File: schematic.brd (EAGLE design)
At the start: 100 x 70 mm, 44 parts, among them U1 ADP3338AKCZ-3.3RL7

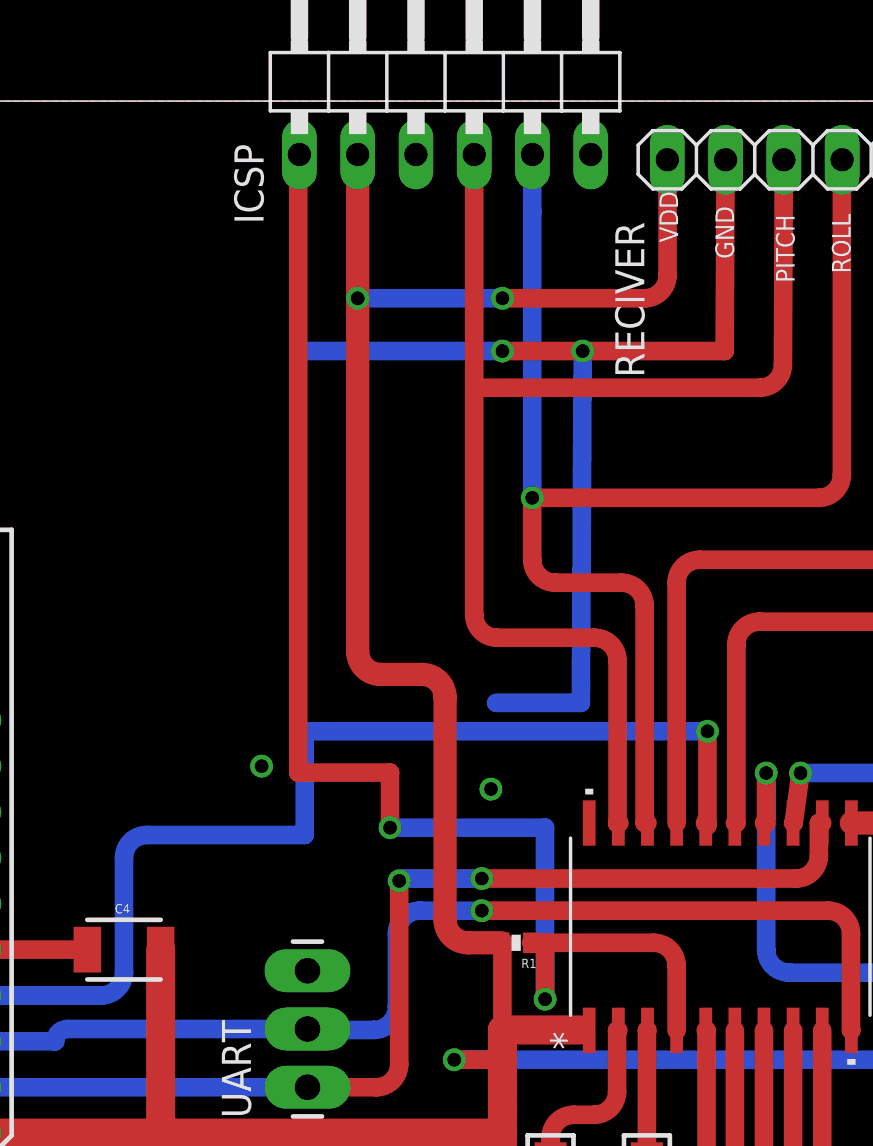
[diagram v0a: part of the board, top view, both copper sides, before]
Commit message: Reversed ICSP pins so programmer will be right way up
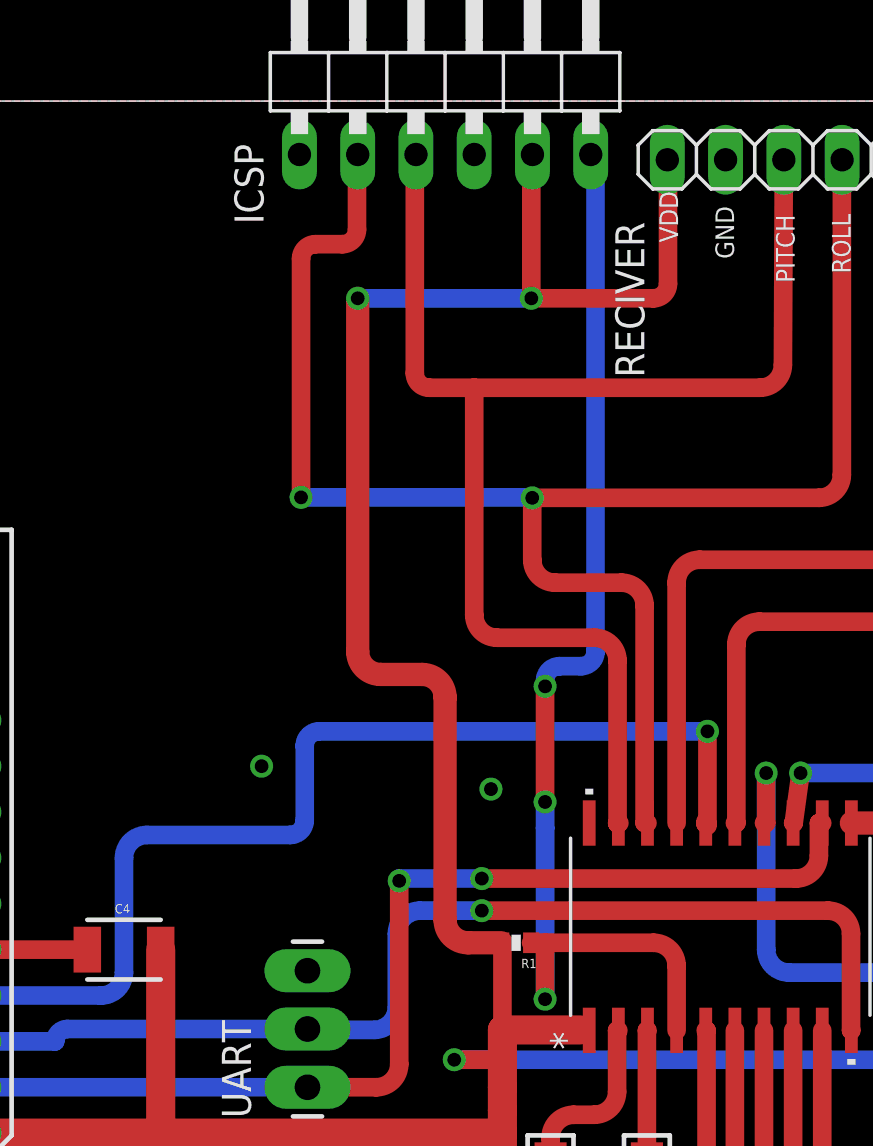
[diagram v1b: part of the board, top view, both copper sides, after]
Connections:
- net GND: now also ICSP.4; no longer ICSP.3
- net LVP: now also ICSP.1; no longer ICSP.6
- net PGC/ROLL: now also ICSP.2; no longer ICSP.5
- net PGD/PITCH: now also ICSP.3; no longer ICSP.4
- net VDD: now also ICSP.5; no longer ICSP.2
- net VPP: now also ICSP.6; no longer ICSP.1
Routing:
- net GND: track 60.0 -> 14.1 mm, vias 6 -> 4
- net PGC/ROLL: track 61.8 -> 73.6 mm, vias 1 -> 2
- net VPP: track 59.7 -> 50.5 mm, vias 2 -> 3
- net PGD/PITCH: track 57.2 -> 59.5 mm
- net XBEE_INT: track 46.1 -> 45.4 mm
- net VDD: track 250.9 -> 250.2 mm
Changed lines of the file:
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@@
 <wire x1="46.4" y1="16.2" x2="46.4" y2="16" width="0.4064" layer="1"/>
 <wire x1="46.5" y1="26.6" x2="46.5" y2="27" width="1.016" layer="1"/>
-<contactref element="ICSP" pad="2"/>
 <wire x1="44" y1="44" x2="43" y2="45" width="1.016" layer="1" curve="90"/>
 <wire x1="43" y1="45" x2="41.19" y2="45" width="1.016" layer="1"/>
@@
 <wire x1="31.6" y1="33" x2="31.6" y2="25.2" width="1.27" layer="1"/>
 <wire x1="31.6" y1="25" x2="31.6" y2="25.2" width="0.6096" layer="1"/>
-<wire x1="40.19" y1="61.4" x2="40.19" y2="67.67" width="1.016" layer="1"/>
 <wire x1="48" y1="16" x2="46.4" y2="16" width="1.27" layer="1"/>
 <wire x1="48" y1="16" x2="48" y2="14.6" width="1.27" layer="1"/>
-<wire x1="53.69" y1="67.44" x2="53.7" y2="68" width="0.8128" layer="1"/>
-<wire x1="53.7" y1="68" x2="53.7" y2="62.4" width="0.8128" layer="1"/>
-<wire x1="53.7" y1="62.4" x2="52.7" y2="61.4" width="0.8128" layer="1" curve="-90"/>
-<wire x1="52.7" y1="61.4" x2="46.5" y2="61.4" width="0.8128" layer="1"/>
-<via x="46.5" y="61.4" extent="1-16" drill="0.6"/>
-<wire x1="46.5" y1="61.4" x2="40.19" y2="61.4" width="0.8128" layer="16"/>
 <via x="40.19" y="61.4" extent="1-16" drill="0.6"/>
 <wire x1="65.05" y1="25.5" x2="65.05" y2="28.2" width="0.8128" layer="1"/>
@@
 <wire x1="74.1" y1="2.4" x2="74" y2="2.4" width="0.254" layer="1"/>
 <wire x1="74" y1="2.4" x2="74" y2="2" width="0.254" layer="1"/>
+<contactref element="ICSP" pad="5"/>
+<wire x1="47.81" y1="67.67" x2="47.76" y2="67.67" width="0.8128" layer="1"/>
+<wire x1="47.76" y1="67.67" x2="47.76" y2="61.4" width="0.8128" layer="1"/>
+<via x="47.76" y="61.4" extent="1-16" drill="0.6" shape="square"/>
+<wire x1="47.76" y1="61.4" x2="40.16" y2="61.4" width="0.8128" layer="16"/>
+<wire x1="40.16" y1="61.4" x2="40.16" y2="61.44" width="0.8128" layer="16"/>
+<wire x1="53.69" y1="67.44" x2="53.72" y2="67.44" width="0.8128" layer="1"/>
+<wire x1="53.72" y1="67.44" x2="53.72" y2="62.035" width="0.8128" layer="1"/>
+<wire x1="53.72" y1="62.035" x2="53.085" y2="61.4" width="0.8128" layer="1" curve="-90"/>
+<wire x1="53.085" y1="61.4" x2="47.72" y2="61.4" width="0.8128" layer="1"/>
+<wire x1="47.76" y1="61.4" x2="47.72" y2="61.4" width="0" layer="19" extent="1-1"/>
+<wire x1="40.19" y1="61.4" x2="40.16" y2="61.4" width="0" layer="19" extent="16-16"/>
 </signal>
 <signal name="VPP">
@@
 <wire x1="53.095" y1="33.3" x2="54.095" y2="32.3" width="0.8128" layer="1" curve="-90"/>
 <wire x1="54.095" y1="32.3" x2="54.095" y2="29.4788" width="0.8128" layer="1"/>
-<contactref element="ICSP" pad="1"/>
-<wire x1="37.65" y1="67.67" x2="37.6" y2="67.67" width="0.8128" layer="1"/>
-<wire x1="37.6" y1="67.67" x2="37.6" y2="40.72" width="0.8128" layer="1"/>
-<wire x1="37.6" y1="40.72" x2="41.6" y2="40.72" width="0.8128" layer="1"/>
-<wire x1="41.6" y1="40.72" x2="41.6" y2="38.32" width="0.8128" layer="1"/>
-<via x="41.6" y="38.32" extent="1-16" drill="0.6" shape="square"/>
-<wire x1="41.6" y1="38.32" x2="48.36" y2="38.32" width="0.8128" layer="16"/>
-<wire x1="48.36" y1="38.32" x2="48.36" y2="30.84" width="0.8128" layer="16"/>
+<wire x1="48.36" y1="38.32" x2="48.36" y2="38.28" width="0.8128" layer="16"/>
 <via x="48.36" y="30.84" extent="1-16" drill="0.6" shape="square"/>
+<wire x1="48.36" y1="38.28" x2="48.36" y2="30.84" width="0.8128" layer="16"/>
 <wire x1="48.36" y1="30.84" x2="48.36" y2="33.3" width="0.8128" layer="1"/>
+<contactref element="ICSP" pad="6"/>
+<wire x1="50.35" y1="67.67" x2="50.56" y2="67.67" width="0.8128" layer="16"/>
+<wire x1="50.56" y1="67.67" x2="50.56" y2="45.995" width="0.8128" layer="16"/>
+<wire x1="50.56" y1="45.995" x2="49.925" y2="45.36" width="0.8128" layer="16" curve="-90"/>
+<wire x1="49.925" y1="45.36" x2="48.995" y2="45.36" width="0.8128" layer="16"/>
+<wire x1="48.995" y1="45.36" x2="48.36" y2="44.725" width="0.8128" layer="16" curve="90"/>
+<wire x1="48.36" y1="44.725" x2="48.36" y2="44.48" width="0.8128" layer="16"/>
+<via x="48.36" y="44.48" extent="1-16" drill="0.6" shape="square"/>
+<wire x1="48.36" y1="44.48" x2="48.36" y2="39.44" width="0.8128" layer="1"/>
+<via x="48.36" y="39.44" extent="1-16" drill="0.6" shape="square"/>
+<wire x1="48.36" y1="39.44" x2="48.36" y2="38.32" width="0.8128" layer="16"/>
 </signal>
 <signal name="N$2">
@@
 <contactref element="D12" pad="C"/>
 <contactref element="UART" pad="3"/>
-<wire x1="50" y1="59.1" x2="49.92" y2="43.76" width="0.8128" layer="16"/>
-<wire x1="49.92" y1="43.76" x2="46.22" y2="43.76" width="0.8128" layer="16"/>
 <wire x1="48" y1="11.4" x2="48" y2="9" width="1.016" layer="1"/>
 <wire x1="48" y1="9" x2="50.19" y2="9" width="1.016" layer="1"/>
 <wire x1="50.19" y1="9" x2="50.19" y2="4.27" width="1.016" layer="1"/>
-<via x="50" y="59.1" extent="1-16" drill="0.6"/>
-<wire x1="50" y1="59.1" x2="46.5" y2="59.1" width="0.8128" layer="1"/>
-<via x="46.5" y="59.1" extent="1-16" drill="0.6"/>
-<wire x1="46.5" y1="59.1" x2="37.65" y2="59.1" width="0.8128" layer="16"/>
-<wire x1="50" y1="59.1" x2="56.19" y2="59.1" width="0.8128" layer="1"/>
-<wire x1="56.19" y1="59.1" x2="56.23" y2="67.44" width="0.8128" layer="1"/>
 <polygon width="0.4064" layer="16">
 <vertex x="0" y="70"/>
@@
 <via x="37" y="9.8" extent="1-16" drill="0.6"/>
 <via x="36" y="41" extent="1-16" drill="0.6"/>
-<contactref element="ICSP" pad="3"/>
-</signal>
-<signal name="LVP">
-<contactref element="ICSP" pad="6"/>
+<contactref element="ICSP" pad="4"/>
 </signal>
 <signal name="M1">
@@
 </signal>
 <signal name="PGD/PITCH">
-<contactref element="ICSP" pad="4"/>
 <contactref element="RECIVER" pad="3"/>
 <contactref element="MAIN_CONTROLLER" pad="19"/>
@@
 <wire x1="46.27" y1="46.6" x2="45.27" y2="47.6" width="0.8128" layer="1" curve="-90"/>
 <wire x1="45.27" y1="47.6" x2="45.27" y2="57.5" width="0.8128" layer="1"/>
-<wire x1="45.27" y1="57.5" x2="45.27" y2="67.67" width="0.8128" layer="1"/>
 <wire x1="45.27" y1="57.5" x2="57.73" y2="57.5" width="0.8128" layer="1"/>
 <wire x1="57.73" y1="57.5" x2="58.73" y2="58.5" width="0.8128" layer="1" curve="90"/>
@@
 <wire x1="51.52" y1="38.48" x2="51.52" y2="38.52" width="0.8128" layer="1"/>
 <wire x1="51.52" y1="38.52" x2="51.6" y2="38.52" width="0.8128" layer="1"/>
+<contactref element="ICSP" pad="3"/>
+<wire x1="45.27" y1="57.5" x2="43.315" y2="57.5" width="0.8128" layer="1"/>
+<wire x1="43.315" y1="57.5" x2="42.68" y2="58.135" width="0.8128" layer="1" curve="-90"/>
+<wire x1="42.68" y1="58.135" x2="42.68" y2="67.6" width="0.8128" layer="1"/>
+<wire x1="42.68" y1="67.6" x2="42.73" y2="67.6" width="0.8128" layer="1"/>
+<wire x1="42.73" y1="67.6" x2="42.73" y2="67.67" width="0.8128" layer="1"/>
 <wire x1="51.52" y1="38.52" x2="51.5" y2="38.5212" width="0" layer="19" extent="1-1"/>
 </signal>
@@
 <wire x1="60.3" y1="52.7" x2="47.8" y2="52.7" width="0.8128" layer="1"/>
 <wire x1="52.825" y1="38.5212" x2="52.7" y2="38.5212" width="0.8128" layer="1"/>
-<contactref element="ICSP" pad="5"/>
-<wire x1="47.81" y1="67.67" x2="47.8" y2="65.19" width="0.8128" layer="16"/>
 <wire x1="61.31" y1="67.44" x2="61.3" y2="68" width="0.8128" layer="1"/>
 <via x="47.8" y="52.7" extent="1-16" drill="0.6"/>
-<wire x1="47.8" y1="52.7" x2="47.8" y2="65.19" width="0.8128" layer="16"/>
 <wire x1="51.7" y1="49" x2="52.7" y2="48" width="0.8128" layer="1" curve="-90"/>
 <wire x1="52.7" y1="48" x2="52.7" y2="38.5212" width="0.8128" layer="1"/>
+<contactref element="ICSP" pad="2"/>
+<wire x1="40.19" y1="67.67" x2="40.16" y2="67.67" width="0.8128" layer="1"/>
+<wire x1="40.16" y1="67.67" x2="40.16" y2="64.395" width="0.8128" layer="1"/>
+<wire x1="40.16" y1="64.395" x2="39.525" y2="63.76" width="0.8128" layer="1" curve="-90"/>
+<wire x1="39.525" y1="63.76" x2="38.355" y2="63.76" width="0.8128" layer="1"/>
+<wire x1="38.355" y1="63.76" x2="37.72" y2="63.125" width="0.8128" layer="1" curve="90"/>
+<wire x1="37.72" y1="63.125" x2="37.72" y2="52.72" width="0.8128" layer="1"/>
+<via x="37.72" y="52.72" extent="1-16" drill="0.6" shape="square"/>
+<wire x1="37.72" y1="52.72" x2="47.8" y2="52.72" width="0.8128" layer="16"/>
+<wire x1="47.8" y1="52.72" x2="47.8" y2="52.7" width="0.8128" layer="16"/>
 </signal>
 <signal name="SCL">
@@
 <wire x1="30" y1="32" x2="30" y2="37" width="0.8128" layer="16"/>
 <wire x1="30" y1="37" x2="31" y2="38" width="0.8128" layer="16" curve="-90"/>
-<wire x1="31" y1="38" x2="37.88" y2="38" width="0.8128" layer="16"/>
-<wire x1="37.88" y1="38" x2="37.88" y2="42.52" width="0.8128" layer="16"/>
-<wire x1="37.88" y1="42.52" x2="55.44" y2="42.52" width="0.8128" layer="16"/>
+<wire x1="31" y1="38" x2="37.245" y2="38" width="0.8128" layer="16"/>
+<wire x1="37.245" y1="38" x2="37.88" y2="38.635" width="0.8128" layer="16" curve="90"/>
+<wire x1="37.88" y1="38.635" x2="37.88" y2="41.885" width="0.8128" layer="16"/>
+<wire x1="37.88" y1="41.885" x2="38.515" y2="42.52" width="0.8128" layer="16" curve="-90"/>
+<wire x1="38.515" y1="42.52" x2="55.44" y2="42.52" width="0.8128" layer="16"/>
 <via x="55.44" y="42.52" extent="1-16" drill="0.6" shape="square"/>
 <wire x1="55.44" y1="42.52" x2="55.44" y2="38.48" width="0.8128" layer="1"/>
@@
 <wire x1="2.9" y1="12.5" x2="6" y2="12.5" width="0.8128" layer="1"/>
 </signal>
+<signal name="LVP">
+<contactref element="ICSP" pad="1"/>
+</signal>
 </signals>
